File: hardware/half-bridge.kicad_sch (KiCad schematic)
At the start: 21 parts, among them J7 Phase_OUT, Q3 AGM015N10LL, Q4 AGM015N10LL, U4 IRS21867S, U5 INA240A2D

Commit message: Capacitors sourced
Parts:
- C20, C21: LCSC (none) -> C28322
- C22, C23: LCSC (none) -> C77020
- C24, C25: LCSC (none) -> C381466
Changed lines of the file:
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@@
+			)
+		)
+		(property "LCSC" "C77020"
+			(at 121.92 107.95 0)
+			(effects
+				(font
+					(size 1.27 1.27)
+				)
+				(hide yes)
 			)
 		)
@@
 			)
 		)
-		(property "Sim.Type" ""
-			(at 99.06 86.36 90)
-			(effects
-				(font
-					(size 1.27 1.27)
-				)
-				(hide yes)
-			)
-		)
 		(pin "2"
 		)
@@
 			)
 		)
-		(property "Sim.Type" ""
-			(at 142.24 81.28 0)
-			(effects
-				(font
-					(size 1.27 1.27)
-				)
-				(hide yes)
-			)
-		)
 		(pin "1"
 		)
@@
 		)
 		(property "LCSC" "C5297508"
-			(at 180.34 90.17 0)
-			(effects
-				(font
-					(size 1.27 1.27)
-				)
-				(hide yes)
-			)
-		)
-		(property "Sim.Type" ""
 			(at 180.34 90.17 0)
 			(effects
@@
 			)
 		)
-		(property "Sim.Type" ""
+		(property "LCSC" "C77020"
 			(at 153.67 115.57 90)
 			(effects
@@
 		)
 		(property "Description" "High and Low Side Driver, 600V, 4.0/4.0A, SOIC-8"
-			(at 68.58 77.47 0)
-			(effects
-				(font
-					(size 1.27 1.27)
-				)
-				(hide yes)
-			)
-		)
-		(property "Sim.Type" ""
 			(at 68.58 77.47 0)
 			(effects
@@
 			)
 		)
-		(property "Sim.Type" ""
-			(at 160.02 102.87 0)
-			(effects
-				(font
-					(size 1.27 1.27)
-				)
-				(hide yes)
-			)
-		)
 		(pin "2"
 		)
@@
 			)
 		)
-		(property "Sim.Type" ""
-			(at 153.67 81.28 90)
-			(effects
-				(font
-					(size 1.27 1.27)
-				)
-				(hide yes)
-			)
-		)
 		(pin "2"
 		)
@@
 			)
 		)
-		(property "Sim.Type" ""
+		(property "LCSC" "C28322"
 			(at 80.01 77.47 0)
 			(effects
@@
 			)
 		)
-		(property "Sim.Type" ""
+		(property "LCSC" "C28322"
 			(at 50.8 63.5 0)
 			(effects
@@
 			)
 		)
-		(property "Sim.Type" ""
-			(at 127 121.92 0)
-			(effects
-				(font
-					(size 1.27 1.27)
-				)
-				(hide yes)
-			)
-		)
 		(pin "3"
 		)
@@
 		(property "Description" "Resistor"
 			(at 170.18 90.17 0)
-			(effects
-				(font
-					(size 1.27 1.27)
-				)
-				(hide yes)
-			)
-		)
-		(property "Sim.Type" ""
-			(at 170.18 90.17 90)
 			(effects
 				(font
@@
 			)
 		)
-		(property "Sim.Type" ""
+		(property "LCSC" "C381466"
 			(at 190.5 80.01 0)
 			(effects
@@
 			)
 		)
-		(property "Sim.Type" ""
+		(property "LCSC" "C381466"
 			(at 199.39 80.01 0)
 			(effects
@@
 			)
 		)
-		(property "Sim.Type" ""
-			(at 147.32 102.87 0)
-			(effects
-				(font
-					(size 1.27 1.27)
-				)
-				(hide yes)
-			)
-		)
 		(pin "2"
 		)
@@
 			)
 		)
-		(property "Sim.Type" ""
-			(at 92.71 82.55 90)
-			(effects
-				(font
-					(size 1.27 1.27)
-				)
-				(hide yes)
-			)
-		)
 		(pin "1"
 		)
@@
 			)
 		)
-		(property "Sim.Type" ""
-			(at 170.18 73.66 90)
-			(effects
-				(font
-					(size 1.27 1.27)
-				)
-				(hide yes)
-			)
-		)
 		(pin "2"
 		)
@@
 			)
 		)
-		(property "Sim.Type" ""
-			(at 99.06 99.06 0)
-			(effects
-				(font
-					(size 1.27 1.27)
-				)
-				(hide yes)
-			)
-		)
 		(pin "2"
 		)
@@
 			(at 180.34 73.66 0)
 			(effects
-				(font
-					(size 1.27 1.27)
-				)
-				(hide yes)
-			)
-		)
-		(property "Sim.Type" ""
-			(at 180.34 73.66 0)
-			(effects

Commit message: Sourcing complete
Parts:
- D4: LCSC (none) -> C552825
- L2: value L_Ferrite -> 1k@100MHz; LCSC (none) -> C76883
- Q3, Q4: value AGM015N10LL -> IPT015N10N5; LCSC C5297508 -> C108964
- R18, R24, R25: LCSC (none) -> C2930253
- R19: LCSC (none) -> C17756
- R20: LCSC (none) -> C114762
- R21, R23: LCSC (none) -> C185446
- U4: LCSC (none) -> C52290
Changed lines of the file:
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@@
+			)
+		)
+		(property "LCSC" "C17756"
+			(at 99.06 86.36 0)
+			(effects
+				(font
+					(size 1.27 1.27)
+				)
+				(hide yes)
 			)
 		)
@@
 			)
 		)
-		(property "Value" "AGM015N10LL"
+		(property "Value" "IPT015N10N5"
 			(at 174.752 85.09 0)
 			(effects
@@
 			)
 		)
-		(property "LCSC" "C5297508"
+		(property "LCSC" "C108964"
 			(at 180.34 90.17 0)
 			(effects
@@
 		(on_board yes)
 		(dnp no)
-		(fields_autoplaced yes)
 		(property "Reference" "L2"
 			(at 114.3 99.06 90)
@@
 			)
 		)
-		(property "Value" "L_Ferrite"
-			(at 114.3 101.6 90)
+		(property "Value" "1k@100MHz"
+			(at 115.57 101.346 90)
 			(effects
 				(font
@@
 		(property "Description" "Inductor with ferrite core"
 			(at 114.3 105.41 0)
+			(effects
+				(font
+					(size 1.27 1.27)
+				)
+				(hide yes)
+			)
+		)
+		(property "LCSC" "C76883"
+			(at 114.3 105.41 90)
 			(effects
 				(font
@@
 			)
 		)
+		(property "LCSC" "C52290"
+			(at 68.58 77.47 0)
+			(effects
+				(font
+					(size 1.27 1.27)
+				)
+				(hide yes)
+			)
+		)
 		(pin "6"
 		)
@@
 			)
 		)
+		(property "LCSC" "C185446"
+			(at 160.02 102.87 0)
+			(effects
+				(font
+					(size 1.27 1.27)
+				)
+				(hide yes)
+			)
+		)
 		(pin "2"
 		)
@@
 			)
 		)
+		(property "LCSC" "C2930253"
+			(at 170.18 90.17 90)
+			(effects
+				(font
+					(size 1.27 1.27)
+				)
+				(hide yes)
+			)
+		)
 		(pin "2"
 		)
@@
 			)
 		)
+		(property "LCSC" "C185446"
+			(at 147.32 102.87 0)
+			(effects
+				(font
+					(size 1.27 1.27)
+				)
+				(hide yes)
+			)
+		)
 		(pin "2"
 		)
@@
 			)
 		)
+		(property "LCSC" "C552825"
+			(at 74.93 64.77 0)
+			(effects
+				(font
+					(size 1.27 1.27)
+				)
+				(hide yes)
+			)
+		)
 		(pin "1"
 		)
@@
 			)
 		)
+		(property "LCSC" "C2930253"
+			(at 92.71 82.55 90)
+			(effects
+				(font
+					(size 1.27 1.27)
+				)
+				(hide yes)
+			)
+		)
 		(pin "1"
 		)
@@
 			)
 		)
+		(property "LCSC" "C2930253"
+			(at 170.18 73.66 90)
+			(effects
+				(font
+					(size 1.27 1.27)
+				)
+				(hide yes)
+			)
+		)
 		(pin "2"
 		)
@@
 			)
 		)
+		(property "LCSC" "C114762"
+			(at 99.06 99.06 0)
+			(effects
+				(font
+					(size 1.27 1.27)
+				)
+				(hide yes)
+			)
+		)
 		(pin "2"
 		)
@@
 			)
 		)
-		(property "Value" "AGM015N10LL"
+		(property "Value" "IPT015N10N5"
 			(at 174.752 68.58 0)
 			(effects
@@
 			)
 		)
-		(property "LCSC" "C5297508"
+		(property "LCSC" "C108964"
 			(at 180.34 73.66 0)
 			(effects

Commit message: Change power connections to pads instead of holes
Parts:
- J7: footprint MountingHole:MountingHole_5.3mm_M5_DIN965_Pad -> TestPoint:TestPoint_Pad_4.0x4.0mm
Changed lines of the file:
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@@
 			)
 		)
-		(property "Footprint" "MountingHole:MountingHole_5.3mm_M5_DIN965_Pad"
+		(property "Footprint" "TestPoint:TestPoint_Pad_4.0x4.0mm"
 			(at 142.24 81.28 0)
 			(effects

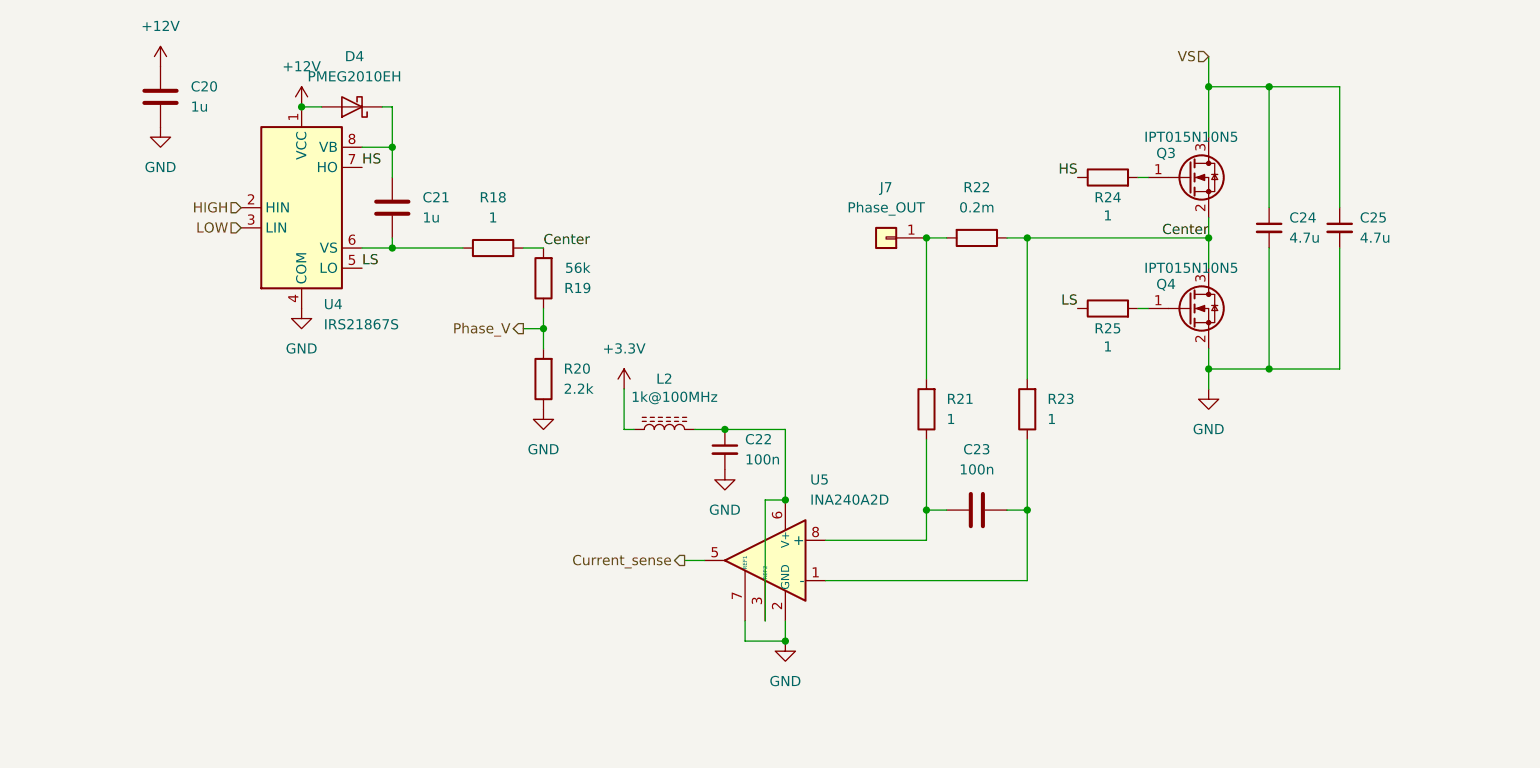
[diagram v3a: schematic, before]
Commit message: Reduce gate MOSFET current
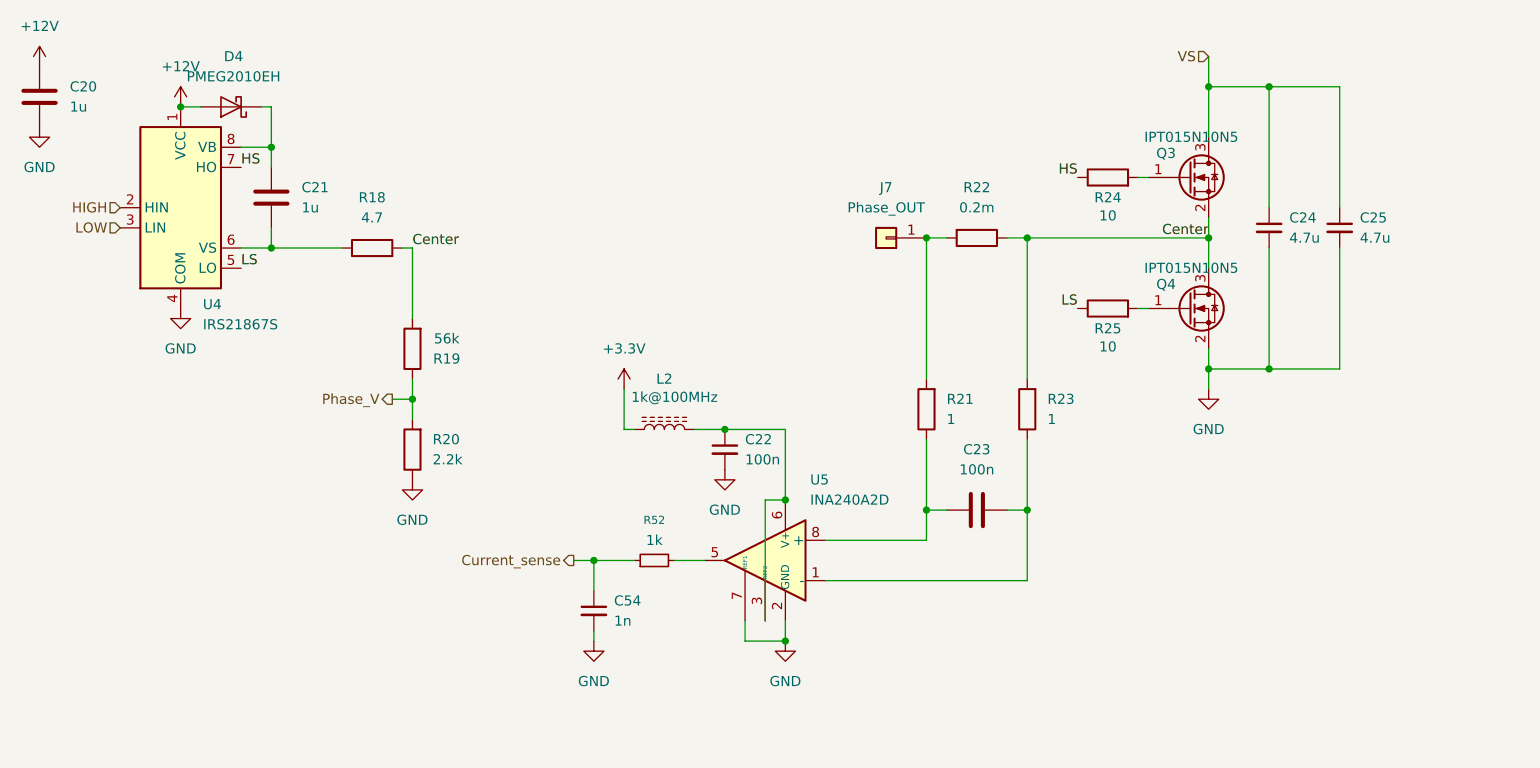
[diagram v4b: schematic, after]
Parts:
- added C54: 1n, symbol Device:C_Small
- added R52: 1k, symbol Device:R_Small
- R18: value 1 -> 4.7; LCSC C2930253 -> C137513
- R24, R25: value 1 -> 10; LCSC C2930253 -> C17415
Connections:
- net Current_sense: now also C54.1, R52.1; no longer U5.5
- net GND: now also C54.2
- new net: R52.2, U5.5
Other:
- moved on the sheet: C20, C21, D4, R18, R19, R20, U4

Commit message: TVS and eletrolythic cap
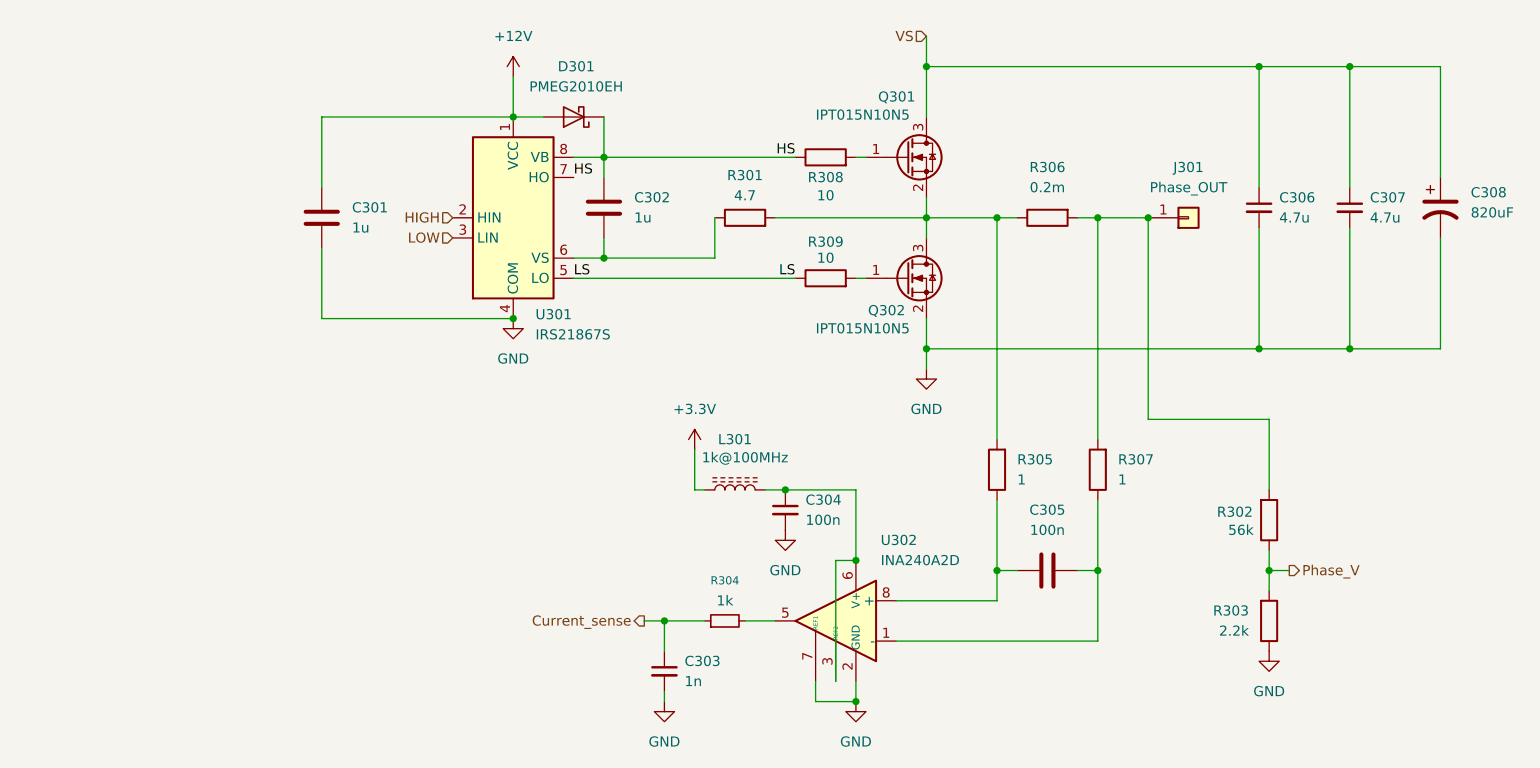
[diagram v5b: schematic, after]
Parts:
- added C308: 820uF, Capacitor_THT:CP_Radial_D18.0mm_P7.50mm, symbol Device:C_Polarized_US
- renumbered C20 to C301, C21 to C302, C54 to C303, C22 to C304, C23 to C305, C24 to C306, C25 to C307, D4 to D301, J7 to J301, L2 to L301, Q3 to Q301, Q4 to Q302, R18 to R301, R19 to R302, R20 to R303, R52 to R304, R21 to R305, R22 to R306, R23 to R307, R24 to R308, R25 to R309, U4 to U301, U5 to U302
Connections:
- net GND: now also C308.2
- net HS: now also C302.1, D301.1 (K), U301.8 (VB)
- net VS: now also C308.1
- net at J301.1 (Pin_1), R306.2: now also R302.2, R307.2; no longer R305.2
- net Center: no longer names the net of Q301.2 (S), Q302.3 (D), R301.2, R306.1
- net Center: now also R305.2; no longer R302.2, R307.2
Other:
- moved on the sheet: C301, C302, C303, C304, C305, C306, C307, D301, J301, L301, Q301, Q302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

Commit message: Change solder wire pads
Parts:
- C303: footprint (none) -> Capacitor_SMD:C_0402_1005Metric
- J301: footprint TestPoint:TestPoint_Pad_4.0x4.0mm -> Connector_Wire:SolderWirePad_1x01_SMD_4x8mm
- R304: footprint (none) -> Resistor_SMD:R_0402_1005Metric
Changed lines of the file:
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@@
 			)
 		)
-		(property "Footprint" "TestPoint:TestPoint_Pad_4.0x4.0mm"
+		(property "Footprint" "Connector_Wire:SolderWirePad_1x01_SMD_4x8mm"
 			(at 180.34 78.74 0)
 			(effects
@@
 			)
 		)
-		(property "Footprint" ""
+		(property "Footprint" "Resistor_SMD:R_0402_1005Metric"
 			(at 121.92 129.54 0)
 			(effects
@@
 			)
 		)
-		(property "Footprint" ""
+		(property "Footprint" "Capacitor_SMD:C_0402_1005Metric"
 			(at 114.3 135.89 0)
 			(effects

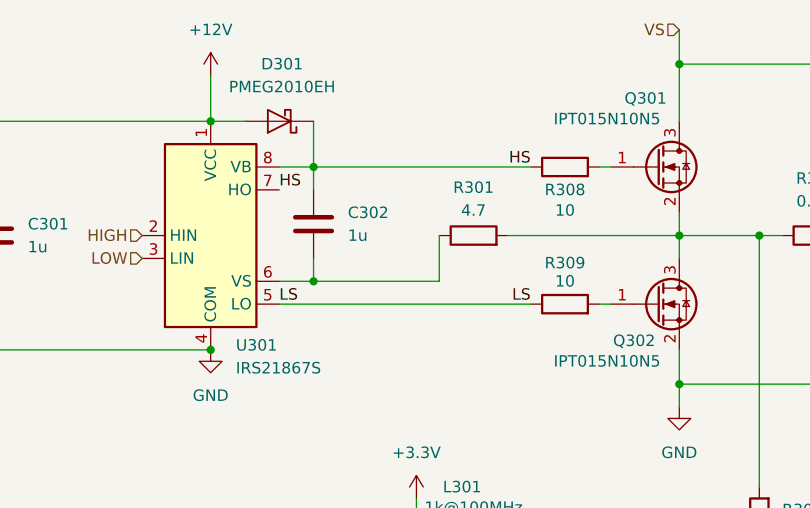
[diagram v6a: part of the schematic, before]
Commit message: Added external analog inputs
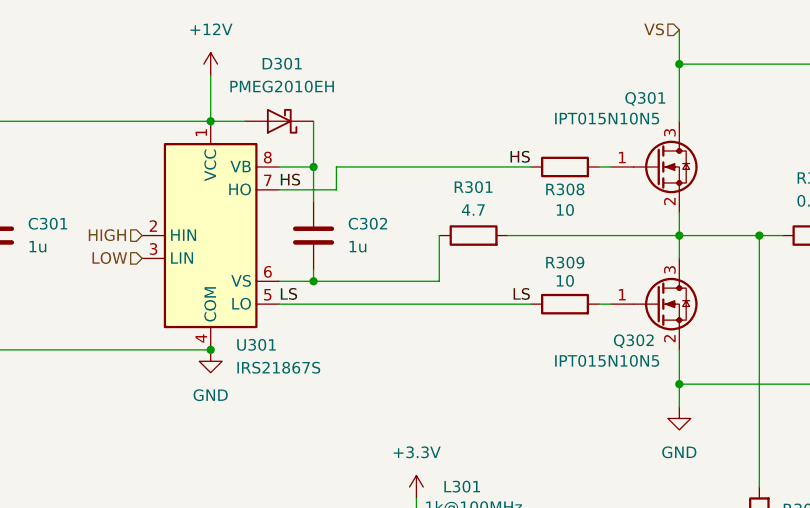
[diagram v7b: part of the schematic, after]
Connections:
- net HS: no longer C302.1, D301.1 (K), U301.8 (VB)
- new net: C302.1, D301.1 (K), U301.8 (VB)
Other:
- moved on the sheet: C302
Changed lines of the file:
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@@
 	(title_block
 		(title "GreenMobi Drive")
-		(date "2025-07-02")
-		(rev "0.1")
+		(date "2025-09-09")
+		(rev "1.0")
 	)
 	(junction
@@
 	)
 	(junction
+		(at 106.68 71.12)
+		(diameter 0)
+		(color 0 0 0 0)
+	)
+	(junction
 		(at 147.32 59.69)
 		(diameter 0)
@@
 	)
 	(junction
-		(at 106.68 71.12)
-		(diameter 0)
-		(color 0 0 0 0)
-	)
-	(junction
 		(at 114.3 129.54)
 		(diameter 0)
@@
 	(wire
 		(pts
+			(xy 106.68 82.55) (xy 106.68 83.82)
+		)
+		(stroke
+			(width 0)
+			(type default)
+		)
+	)
+	(wire
+		(pts
 			(xy 129.54 113.03) (xy 138.43 113.03)
 		)
@@
 	(wire
 		(pts
-			(xy 106.68 83.82) (xy 106.68 81.28)
-		)
-		(stroke
-			(width 0)
-			(type default)
-		)
-	)
-	(wire
-		(pts
 			(xy 135.89 137.16) (xy 135.89 121.92)
 		)
@@
 	(wire
 		(pts
-			(xy 106.68 71.12) (xy 130.81 71.12)
-		)
-		(stroke
-			(width 0)
-			(type default)
-		)
-	)
-	(wire
-		(pts
 			(xy 168.91 78.74) (xy 168.91 106.68)
 		)
@@
 	(wire
 		(pts
+			(xy 109.22 73.66) (xy 109.22 71.12)
+		)
+		(stroke
+			(width 0)
+			(type default)
+		)
+	)
+	(wire
+		(pts
 			(xy 189.23 59.69) (xy 189.23 74.93)
 		)
@@
 	(wire
 		(pts
+			(xy 102.87 73.66) (xy 109.22 73.66)
+		)
+		(stroke
+			(width 0)
+			(type default)
+		)
+	)
+	(wire
+		(pts
+			(xy 109.22 71.12) (xy 130.81 71.12)
+		)
+		(stroke
+			(width 0)
+			(type default)
+		)
+	)
+	(wire
+		(pts
+			(xy 106.68 71.12) (xy 106.68 74.93)
+		)
+		(stroke
+			(width 0)
+			(type default)
+		)
+	)
+	(wire
+		(pts
 			(xy 147.32 59.69) (xy 189.23 59.69)
 		)
@@
 		(pts
 			(xy 95.25 60.96) (xy 95.25 66.04)
-		)
-		(stroke
-			(width 0)
-			(type default)
-		)
-	)
-	(wire
-		(pts
-			(xy 106.68 73.66) (xy 106.68 71.12)
 		)
 		(stroke
@@
 	(symbol
 		(lib_id "Device:C")
-		(at 106.68 77.47 0)
+		(at 106.68 78.74 0)
 		(unit 1)
 		(exclude_from_sim no)
@@
 		(fields_autoplaced yes)
 		(property "Reference" "C302"
-			(at 110.49 76.1999 0)
+			(at 110.49 77.4699 0)
 			(effects
 				(font
@@
 		)
 		(property "Value" "1u"
-			(at 110.49 78.7399 0)
+			(at 110.49 80.0099 0)
 			(effects
 				(font
@@
 		)
 		(property "Footprint" "Capacitor_SMD:C_1206_3216Metric"
-			(at 107.6452 81.28 0)
+			(at 107.6452 82.55 0)
 			(effects
 				(font
@@
 		)
 		(property "Datasheet" "~"
-			(at 106.68 77.47 0)
+			(at 106.68 78.74 0)
 			(effects
 				(font
@@
 		)
 		(property "Description" "Unpolarized capacitor"
-			(at 106.68 77.47 0)
+			(at 106.68 78.74 0)
 			(effects
 				(font
@@
 		)
 		(property "LCSC" "C28322"
-			(at 106.68 77.47 0)
-			(effects
-				(font
+			(at 106.68 78.74 0)
+			(effects
+				(font

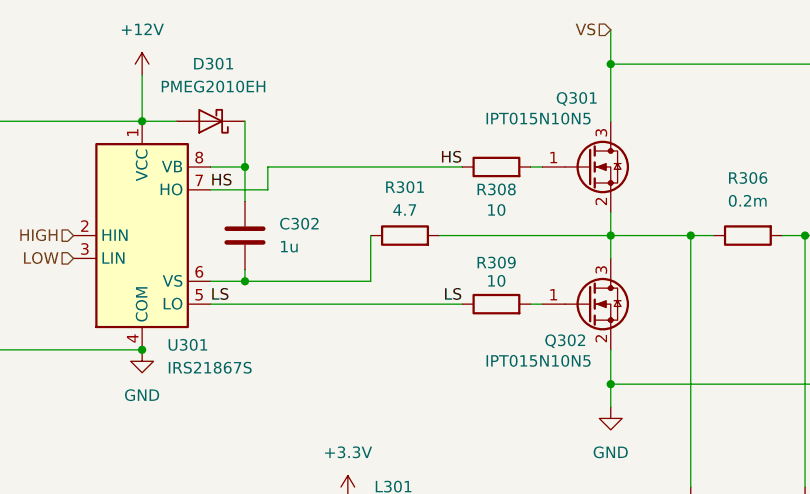
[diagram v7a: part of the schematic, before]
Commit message: Changed bootstrap resistor to 0 Ohm
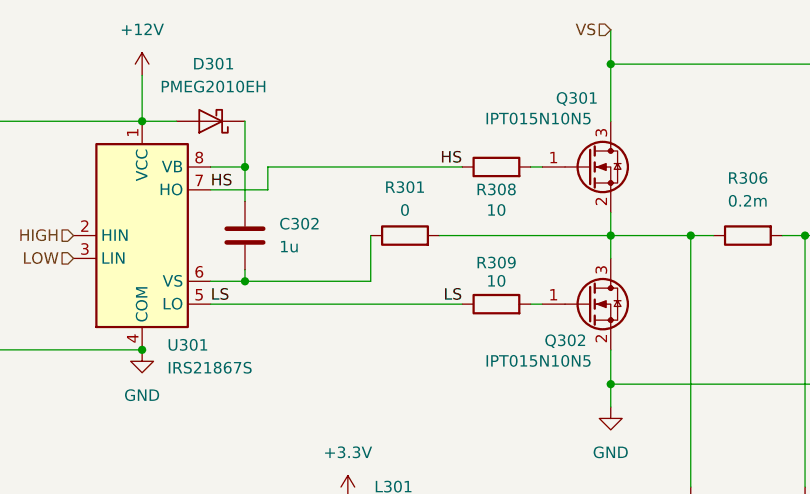
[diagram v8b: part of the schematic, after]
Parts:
- R301: value 4.7 -> 0
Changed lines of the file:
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@@
 			)
 		)
-		(property "Value" "4.7"
+		(property "Value" "0"
 			(at 124.46 75.946 90)
 			(effects
